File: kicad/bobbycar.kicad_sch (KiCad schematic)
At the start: 66 parts, among them J10 BREMSE, J11 CAN2, J12 PROG, J13 LED, J2 IO2, J3 GAS, J4 TFT, J5 Conn_02x08_Odd_Even, J6 Conn_02x08_Odd_Even, J7 BREMSE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

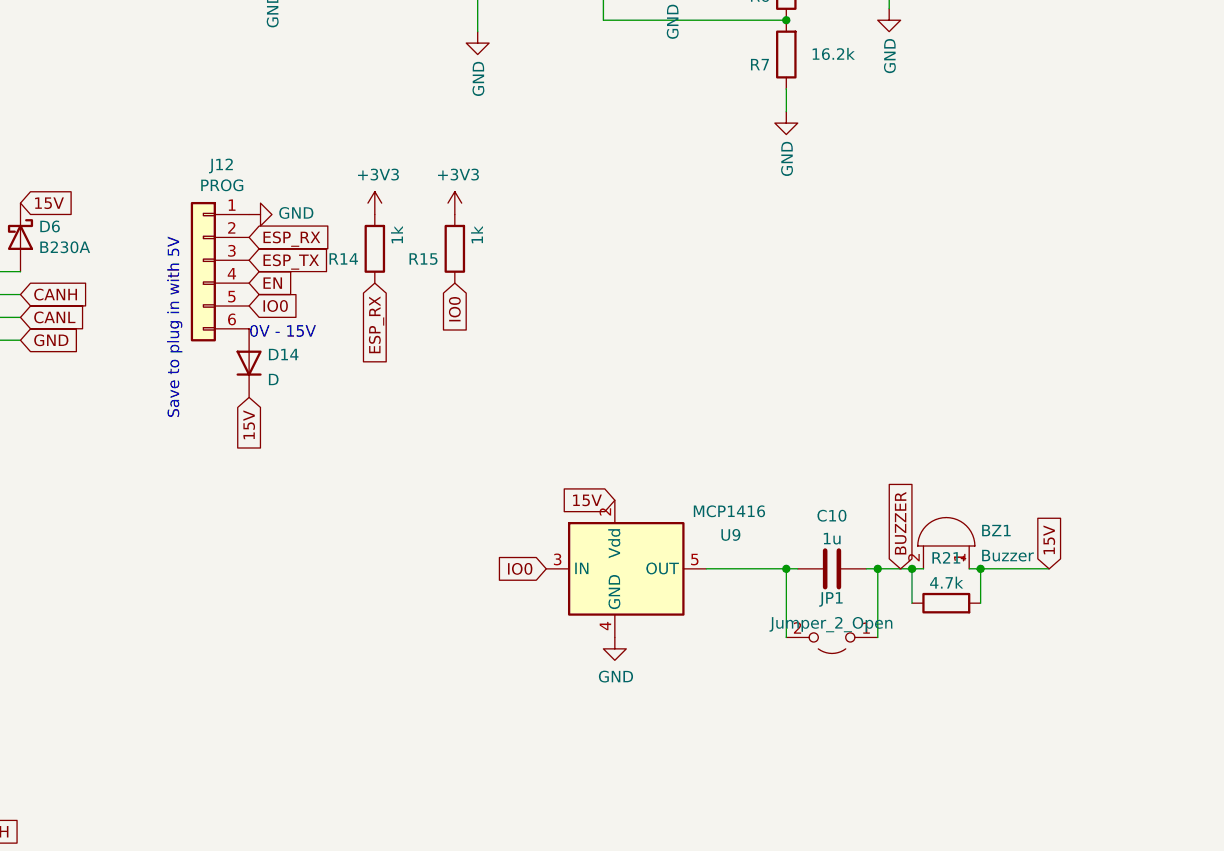
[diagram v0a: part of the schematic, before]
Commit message: Move buzzer stuff to sub-sheet, connect buzzer to GND instead of +15V
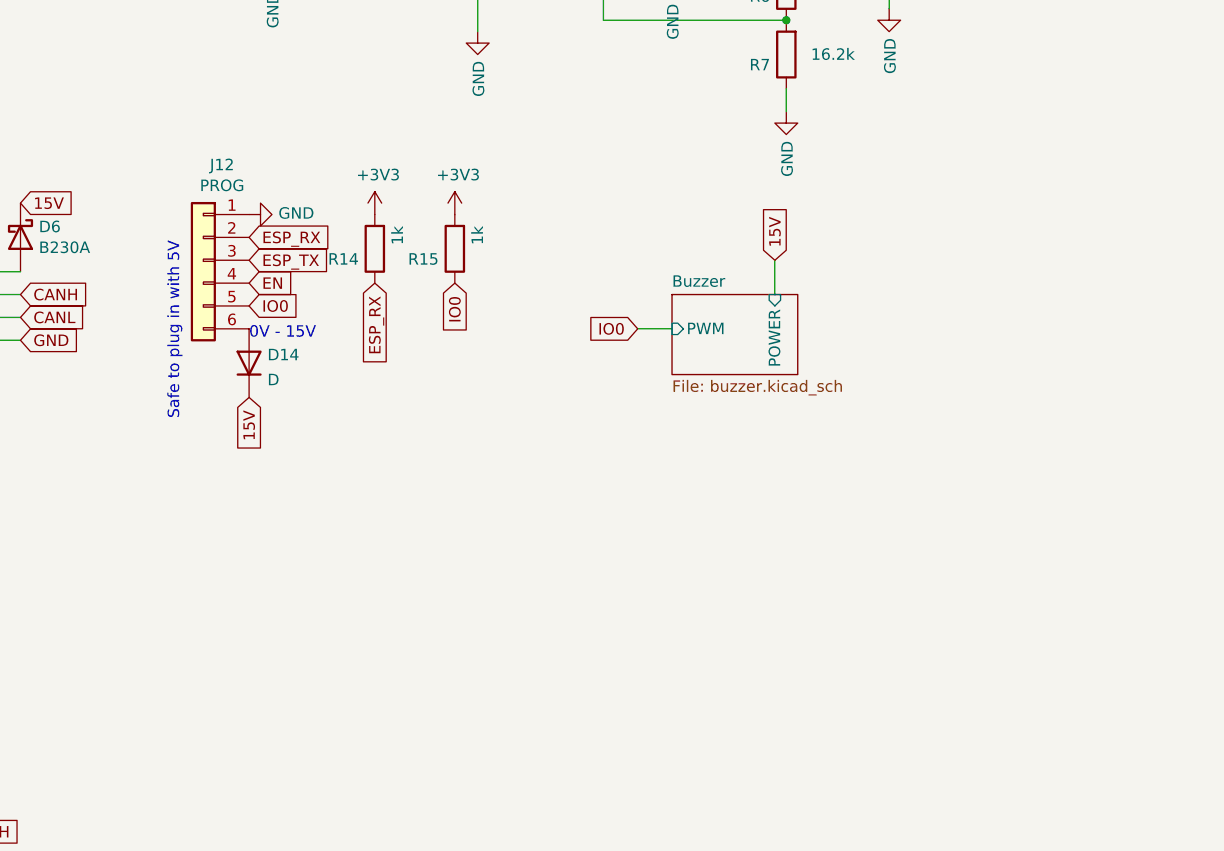
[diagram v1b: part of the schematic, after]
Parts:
- removed BZ1: Buzzer, Capacitor_SMD:CP_Elec_18x22, symbol Device:Buzzer
- removed C10: 1u, Capacitor_SMD:C_0805_2012Metric, symbol Device:C
- removed JP1: Jumper_2_Open, Jumper:SolderJumper-2_P1.3mm_Open_RoundedPad1.0x1.5mm, symbol Jumper:Jumper_2_Open
- removed R21: 4.7k, Resistor_SMD:R_0603_1608Metric, symbol Device:R
- removed U9: MCP1416, Package_TO_SOT_SMD:SOT-23-5, symbol Driver_FET:MCP1416
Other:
- added sheet Buzzer (buzzer.kicad_sch)
- note added: "Safe to plug in with 5V"
- note removed: "Save to plug in with 5V"

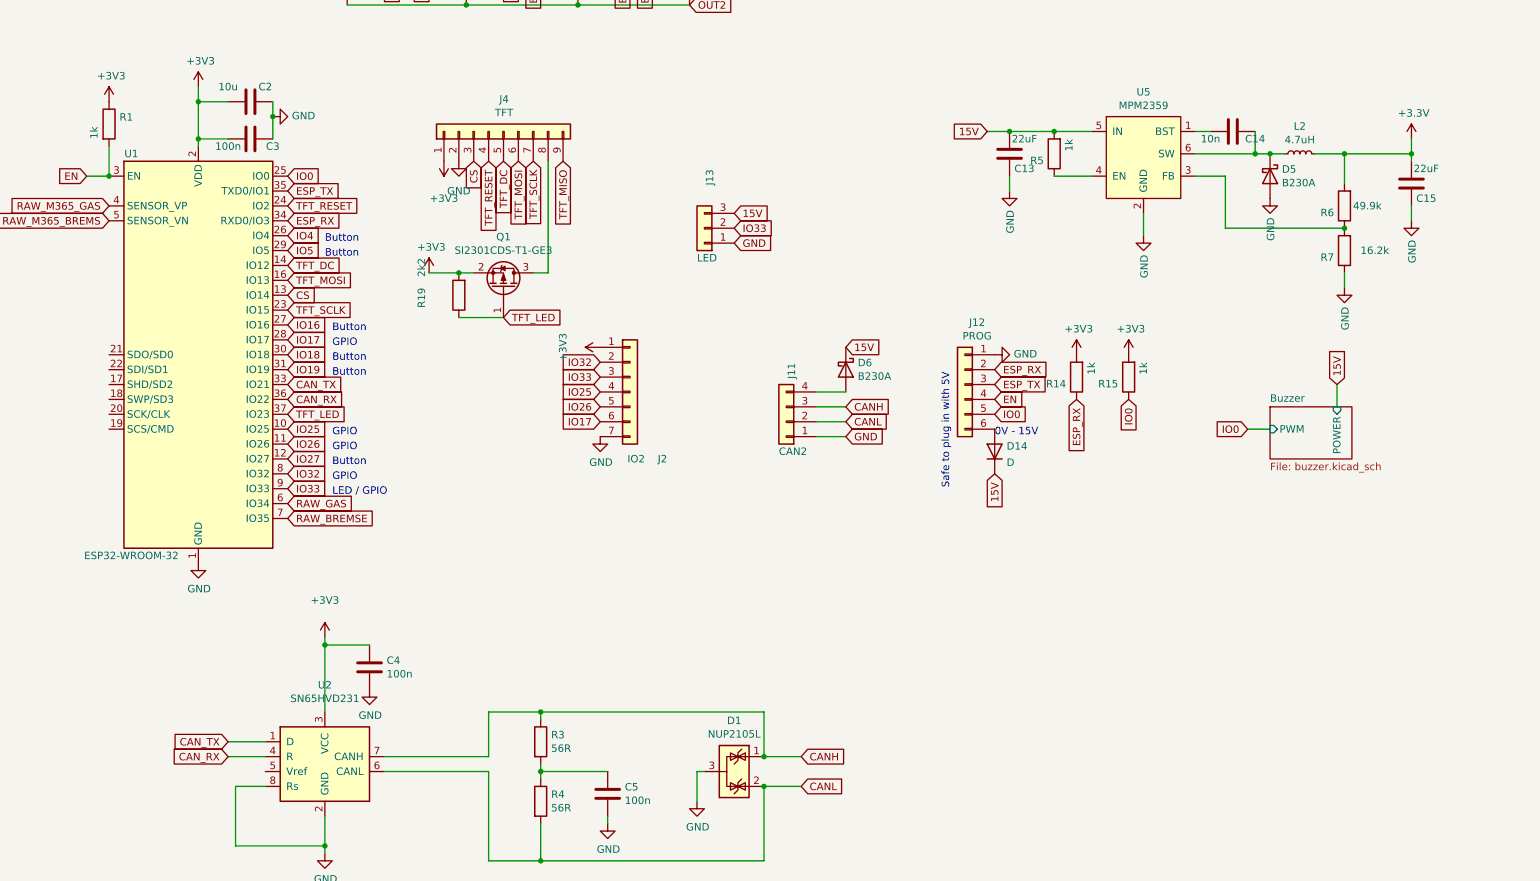
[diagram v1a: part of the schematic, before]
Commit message: Fix some ERC issues, use +3V3 label everywhere
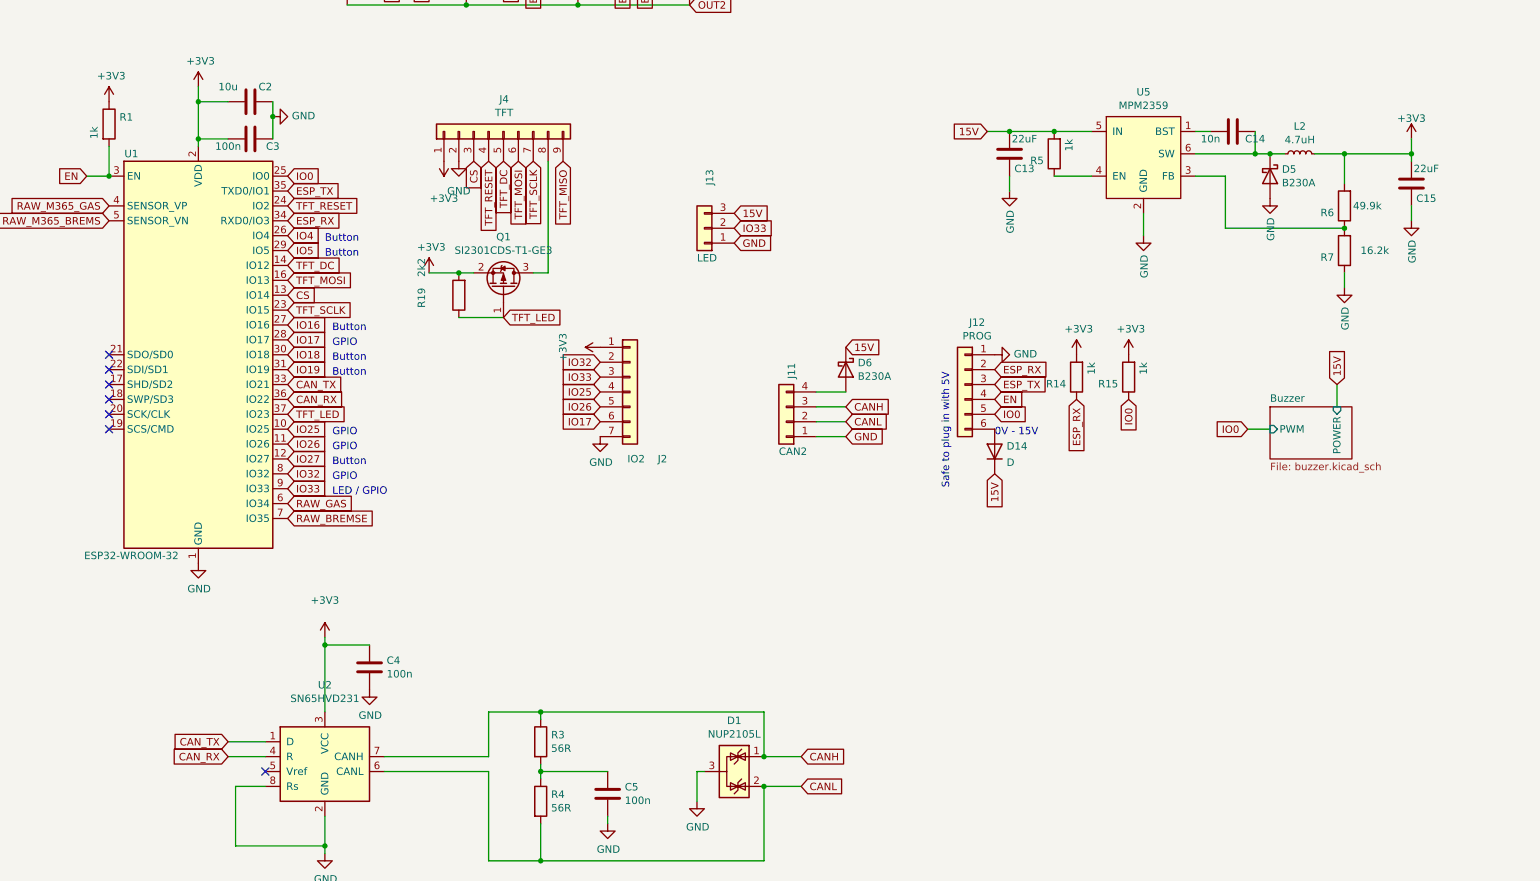
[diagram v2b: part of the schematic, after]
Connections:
- no-connect marks 0 -> 7
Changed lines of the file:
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@@
   (junction (at 246.38 77.47) (diameter 0) (color 0 0 0 0)
   )
+  (no_connect (at 35.56 101.6))
+  (no_connect (at 35.56 106.68))
+  (no_connect (at 35.56 111.76))
+  (no_connect (at 35.56 104.14))
+  (no_connect (at 35.56 109.22))
+  (no_connect (at 35.56 99.06))
+  (no_connect (at 62.23 170.18))
   (wire (pts (xy 391.16 91.44) (xy 391.16 95.25))
     (stroke (width 0) (type default))
@@
     )
   )
-  (symbol (lib_id "power:+3.3V") (at 257.81 62.23 0) (unit 1)
-    (in_bom yes) (on_board yes) (dnp no)
-    (property "Reference" "#PWR0105" (at 257.81 66.04 0)
-      (effects (font (size 1.27 1.27)) hide)
-    )
-    (property "Value" "+3.3V" (at 258.191 57.8358 0)
-      (effects (font (size 1.27 1.27)))
-    )
-    (property "Footprint" "" (at 257.81 62.23 0)
-      (effects (font (size 1.27 1.27)) hide)
-    )
-    (property "Datasheet" "" (at 257.81 62.23 0)
-      (effects (font (size 1.27 1.27)) hide)
-    )
-    (pin "1")
-    (instances
-      (project "bobbycar"
-        (path "/477311b9-8f81-40c8-9c55-fd87e287247a"
-          (reference "#PWR0105") (unit 1)
-        )
-      )
-    )
-  )
   (symbol (lib_id "Device:C") (at 189.23 64.77 180) (unit 1)
     (in_bom yes) (on_board yes) (dnp no)
@@
       (effects (font (size 1.27 1.27)) hide)
     )
+    (property "Sim.Device" "D" (at 186.69 115.57 0)
+      (effects (font (size 1.27 1.27)) hide)
+    )
+    (property "Sim.Pins" "1=K 2=A" (at 186.69 115.57 0)
+      (effects (font (size 1.27 1.27)) hide)
+    )
     (pin "1")
     (pin "2")
@@
         )
       )
+    )
+  )
+  (symbol (lib_id "power:+3V3") (at 257.81 62.23 0) (unit 1)
+    (in_bom yes) (on_board yes) (dnp no) (fields_autoplaced)
+    (property "Reference" "#PWR010" (at 257.81 66.04 0)
+      (effects (font (size 1.27 1.27)) hide)
+    )
+    (property "Value" "+3V3" (at 257.81 58.7281 0)
+      (effects (font (size 1.27 1.27)))
+    )
+    (property "Footprint" "" (at 257.81 62.23 0)
+      (effects (font (size 1.27 1.27)) hide)
+    )
+    (property "Datasheet" "" (at 257.81 62.23 0)
+      (effects (font (size 1.27 1.27)) hide)
+    )
+    (pin "1")
+    (instances
+      (project "bobbycar"
+        (path "/477311b9-8f81-40c8-9c55-fd87e287247a"
+          (reference "#PWR010") (unit 1)
+        )
+      )

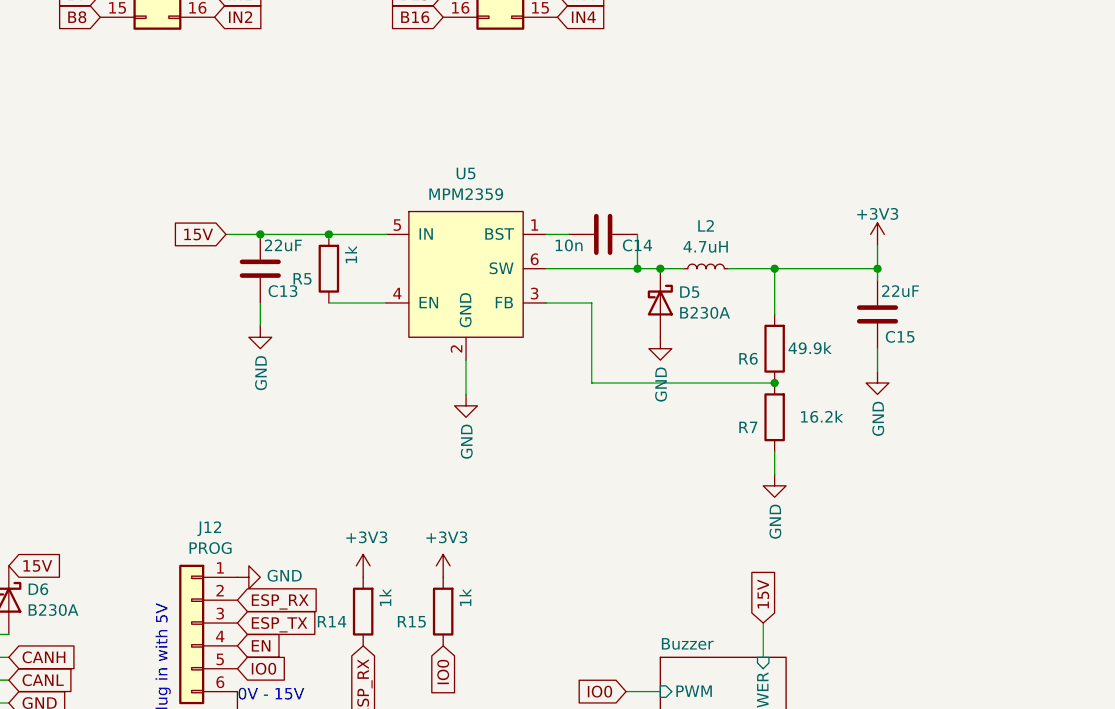
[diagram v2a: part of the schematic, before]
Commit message: Move 3V3 supply to sub-sheet
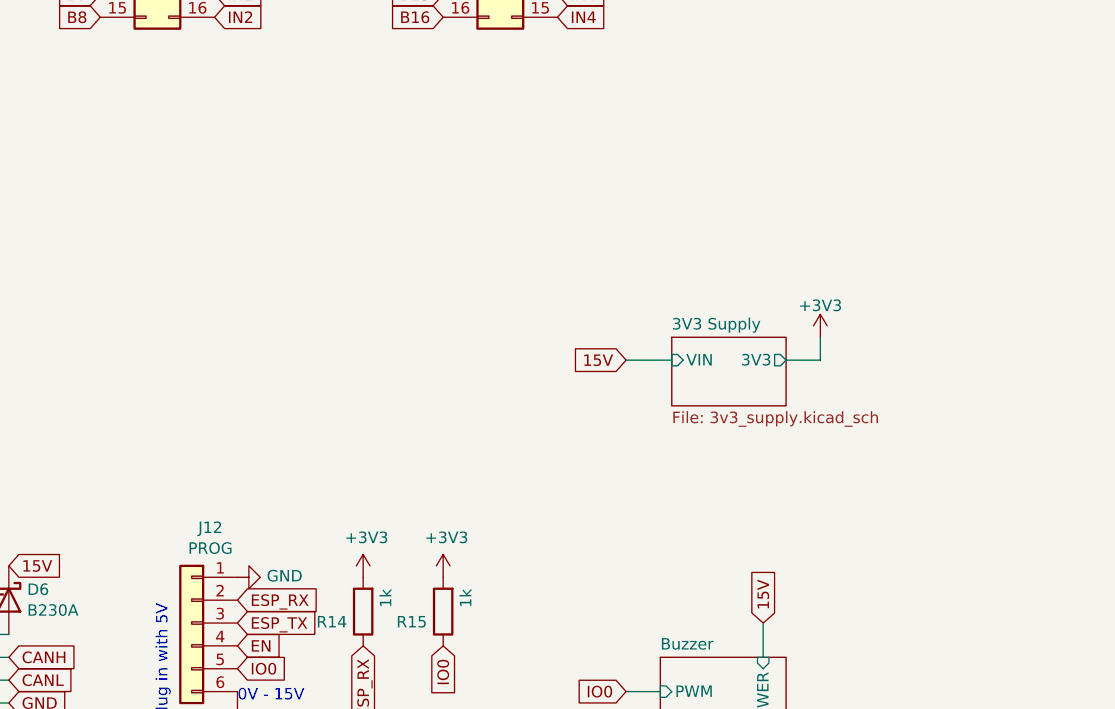
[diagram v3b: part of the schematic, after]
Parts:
- removed C13, C15: 22uF, Capacitor_SMD:C_0805_2012Metric, symbol Device:C
- removed C14: 10n, Capacitor_SMD:C_0603_1608Metric, symbol Device:C
- removed D5: B230A, Diode_SMD:D_SMA, symbol Diode:B230
- removed L2: 4.7uH, boardcomputer:L_5040, symbol Device:L_Small
- removed R5: 1k, Resistor_SMD:R_0603_1608Metric, symbol Device:R
- removed R6: 49.9k, Resistor_SMD:R_0603_1608Metric, symbol Device:R
- removed R7: 16.2k, Resistor_SMD:R_0603_1608Metric, symbol Device:R
- removed U5: MPM2359, Package_TO_SOT_SMD:SOT-23-6, symbol boardcomputer:MPM2359
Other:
- added sheet 3V3 Supply (3v3_supply.kicad_sch)
